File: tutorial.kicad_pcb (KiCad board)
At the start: 2 copper layers, 174.4 x 164.8 mm, 64 parts

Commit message: modified the pcb some
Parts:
- moved TRRS1 9.19 mm to (214.5, 130.5)
- moved _1 3.21 mm to (210.7, 92.6)
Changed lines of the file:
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@@
 		(fp_line
 			(start -0.35 0)
-			(end -0.35 0.550001)
+			(end -0.35 0.550002)
 			(stroke
 				(width 0.1)
@@
 		(fp_line
 			(start -0.35 0)
-			(end -0.35 0.550001)
+			(end -0.35 0.550002)
 			(stroke
 				(width 0.1)
@@
 		(fp_line
 			(start -0.35 0)
-			(end -0.35 0.550001)
+			(end -0.35 0.550002)
 			(stroke
 				(width 0.1)
@@
 		(fp_line
 			(start -0.35 0)
-			(end -0.35 0.550001)
+			(end -0.35 0.550002)
 			(stroke
 				(width 0.1)
@@
 		(fp_line
 			(start -0.35 0)
-			(end -0.35 0.550001)
+			(end -0.35 0.550002)
 			(stroke
 				(width 0.1)
@@
 		(fp_line
 			(start -0.35 0)
-			(end -0.35 0.550001)
+			(end -0.35 0.550002)
 			(stroke
 				(width 0.1)
@@
 		(fp_line
 			(start -0.35 0)
-			(end -0.35 0.550001)
+			(end -0.35 0.550002)
 			(stroke
 				(width 0.1)
@@
 		(fp_line
 			(start -0.35 0)
-			(end -0.35 0.550001)
+			(end -0.35 0.550002)
 			(stroke
 				(width 0.1)
@@
 		(fp_line
 			(start -0.35 0)
-			(end -0.35 0.550001)
+			(end -0.35 0.550002)
 			(stroke
 				(width 0.1)
@@
 		(fp_line
 			(start -0.35 0)
-			(end -0.35 0.550001)
+			(end -0.35 0.550002)
 			(stroke
 				(width 0.1)
@@
 		(fp_line
 			(start -0.35 0)
-			(end -0.35 0.550001)
+			(end -0.35 0.550002)
 			(stroke
 				(width 0.1)
@@
 		(fp_line
 			(start -0.35 0)
-			(end -0.35 0.550001)
+			(end -0.35 0.550002)
 			(stroke
 				(width 0.1)
@@
 		(fp_line
 			(start -0.35 0)
-			(end -0.35 0.550001)
+			(end -0.35 0.550002)
 			(stroke
 				(width 0.1)
@@
 		(fp_line
 			(start -0.35 0)
-			(end -0.35 0.550001)
+			(end -0.35 0.550002)
 			(stroke
 				(width 0.1)
@@
 		(fp_line
 			(start -0.35 0)
-			(end -0.35 0.550001)
+			(end -0.35 0.550002)
 			(stroke
 				(width 0.1)
@@
 		(fp_line
 			(start -0.35 0)
-			(end -0.35 0.550001)
+			(end -0.35 0.550002)
 			(stroke
 				(width 0.1)
@@
 	(footprint "RPi_Pico_SMD_TH"
 		(layer "F.Cu")
-		(at 209.404157 95.553697 -15)
+		(at 210.730194 92.627828 -15)
 		(property "Reference" "_1"
 			(at 0 0 0)
@@
 			)
 		)
-		(fp_text user "Copper Keepouts shown on Dwgs layer"
-			(at 0.1 -30.2 0)
-			(layer "Cmts.User")
-			(effects
-				(font
-					(size 1 1)
-					(thickness 0.15)
-				)
-			)
-		)
 		(fp_text user "${REFERENCE}"
 			(at 0 0 180)
@@
 		(fp_line
 			(start -0.35 0)
-			(end -0.35 0.550001)
+			(end -0.35 0.550002)
 			(stroke
 				(width 0.1)
@@
 		(fp_line
 			(start -0.35 0)
-			(end -0.35 0.550001)
+			(end -0.35 0.550002)
 			(stroke
 				(width 0.1)
@@
 		(fp_line
 			(start -0.35 0)
-			(end -0.35 0.550001)
+			(end -0.35 0.550002)
 			(stroke
 				(width 0.1)
@@
 		(fp_line
 			(start -0.35 0)
-			(end -0.35 0.550001)
+			(end -0.35 0.550002)
 			(stroke
 				(width 0.1)
@@
 		(fp_line
 			(start -0.35 0)
-			(end -0.35 0.550001)
+			(end -0.35 0.550002)
 			(stroke
 				(width 0.1)
@@
 		(fp_line
 			(start -0.35 0)
-			(end -0.35 0.550001)
+			(end -0.35 0.550002)
 			(stroke
 				(width 0.1)
@@
 		(fp_line
 			(start -0.35 0)
-			(end -0.35 0.550001)
+			(end -0.35 0.550002)
 			(stroke
 				(width 0.1)
@@
 		(fp_line
 			(start -0.35 0)
-			(end -0.35 0.550001)
+			(end -0.35 0.550002)
 			(stroke
 				(width 0.1)
@@
 		(fp_line
 			(start -0.35 0)
-			(end -0.35 0.550001)
+			(end -0.35 0.550002)
 			(stroke
 				(width 0.1)
@@
 		(fp_line
 			(start -0.35 0)
-			(end -0.35 0.550001)
+			(end -0.35 0.550002)
 			(stroke
 				(width 0.1)
@@
 		(fp_line
 			(start -0.35 0)
-			(end -0.35 0.550001)
+			(end -0.35 0.550002)
 			(stroke
 				(width 0.1)
@@
 		(fp_line
 			(start -0.35 0)
-			(end -0.35 0.550001)
+			(end -0.35 0.550002)
 			(stroke
 				(width 0.1)
@@
 	(footprint "ceoloide:trrs_pj320a (reversible, symmetric)"
 		(layer "F.Cu")
-		(at 209.306933 122.962465 -105)
+		(at 214.495679 130.54985 -105)
 		(property "Reference" "TRRS1"
 			(at 0 14.2 -105)
@@
 		)
 		(pad "2" thru_hole oval
-			(at 2.299999 3.2 255)
+			(at 2.299998 3.2 255)
 			(size 1.6 2.2)
 			(drill oval 0.9 1.5)
@@
 		(fp_line
 			(start -0.35 0)
-			(end -0.35 0.550001)
+			(end -0.35 0.550002)
 			(stroke
 				(width 0.1)
@@
 		(fp_line
 			(start -0.35 0)
-			(end -0.35 0.550001)
+			(end -0.35 0.550002)
 			(stroke
 				(width 0.1)
@@
 		(fp_line
 			(start -0.35 0)
-			(end -0.35 0.550001)
+			(end -0.35 0.550002)
 			(stroke
 				(width 0.1)
@@
 		(fp_line
 			(start -0.35 0)
-			(end -0.35 0.550001)
+			(end -0.35 0.550002)
 			(stroke
 				(width 0.1)
@@
 		(fp_line
 			(start -0.35 0)
-			(end -0.35 0.550001)
+			(end -0.35 0.550002)
 			(stroke
 				(width 0.1)
@@
 		(fp_line
 			(start -0.35 0)
-			(end -0.35 0.550001)
+			(end -0.35 0.550002)
 			(stroke
 				(width 0.1)
@@
 		(fp_line
 			(start -0.35 0)
-			(end -0.35 0.550001)
+			(end -0.35 0.550002)
 			(stroke
 				(width 0.1)
@@
 		(fp_line
 			(start -0.35 0)
-			(end -0.35 0.550001)
+			(end -0.35 0.550002)
 			(stroke
 				(width 0.1)
@@
 		(fp_line
 			(start -0.35 0)
-			(end -0.35 0.550001)
+			(end -0.35 0.550002)
 			(stroke
 				(width 0.1)
@@
 		(fp_line
 			(start -0.35 0)
-			(end -0.35 0.550001)
+			(end -0.35 0.550002)
 			(stroke
 				(width 0.1)
@@
 		(fp_line
 			(start -0.35 0)
-			(end -0.35 0.550001)
+			(end -0.35 0.550002)
 			(stroke
 				(width 0.1)
@@
 		(fp_line
 			(start -0.35 0)
-			(end -0.35 0.550001)
+			(end -0.35 0.550002)
 			(stroke
 				(width 0.1)
@@
 		(fp_line
 			(start -0.35 0)
-			(end -0.35 0.550001)
+			(end -0.35 0.550002)
 			(stroke
 				(width 0.1)
@@
 		(fp_line
 			(start -0.35 0)
-			(end -0.35 0.550001)
+			(end -0.35 0.550002)
 			(stroke
 				(width 0.1)
@@
 		(fp_line
 			(start -0.35 0)
-			(end -0.35 0.550001)
+			(end -0.35 0.550002)
 			(stroke
 				(width 0.1)
@@
 		(fp_line
 			(start -0.35 0)
-			(end -0.35 0.550001)
+			(end -0.35 0.550002)
 			(stroke
 				(width 0.1)
@@
 		(fp_line
 			(start -0.35 0)
-			(end -0.35 0.550001)
+			(end -0.35 0.550002)
 			(stroke
 				(width 0.1)
@@
 		(fp_line
 			(start -0.35 0)
-			(end -0.35 0.550001)
+			(end -0.35 0.550002)
 			(stroke
 				(width 0.1)
@@
 		(fp_line
 			(start -0.35 0)
-			(end -0.35 0.550001)
+			(end -0.35 0.550002)
 			(stroke
 				(width 0.1)
@@
 		(fp_line
 			(start -0.35 0)
-			(end -0.35 0.550001)
+			(end -0.35 0.550002)
 			(stroke
 				(width 0.1)
@@
 		(fp_line
 			(start -0.35 0)
-			(end -0.35 0.550001)
+			(end -0.35 0.550002)
 			(stroke
 				(width 0.1)
@@
 		(fp_line
 			(start -0.35 0)
-			(end -0.35 0.550001)
+			(end -0.35 0.550002)
 			(stroke
 				(width 0.1)
@@
 		(fp_line
 			(start -0.35 0)
-			(end -0.35 0.550001)
+			(end -0.35 0.550002)
 			(stroke
 				(width 0.1)
@@
 		(fp_line
 			(start -0.35 0)
-			(end -0.35 0.550001)
+			(end -0.35 0.550002)
 			(stroke
 				(width 0.1)
@@
 		(fp_line
 			(start -0.35 0)
-			(end -0.35 0.550001)
+			(end -0.35 0.550002)
 			(stroke
 				(width 0.1)
@@
 		(fp_line
 			(start -0.35 0)
-			(end -0.35 0.550001)
+			(end -0.35 0.550002)
 			(stroke
 				(width 0.1)
@@
 		(fp_line
 			(start -0.35 0)
-			(end -0.35 0.550001)
+			(end -0.35 0.550002)
 			(stroke
 				(width 0.1)
@@
 		(fp_line
 			(start -0.35 0)
-			(end -0.35 0.550001)
+			(end -0.35 0.550002)
 			(stroke
 				(width 0.1)

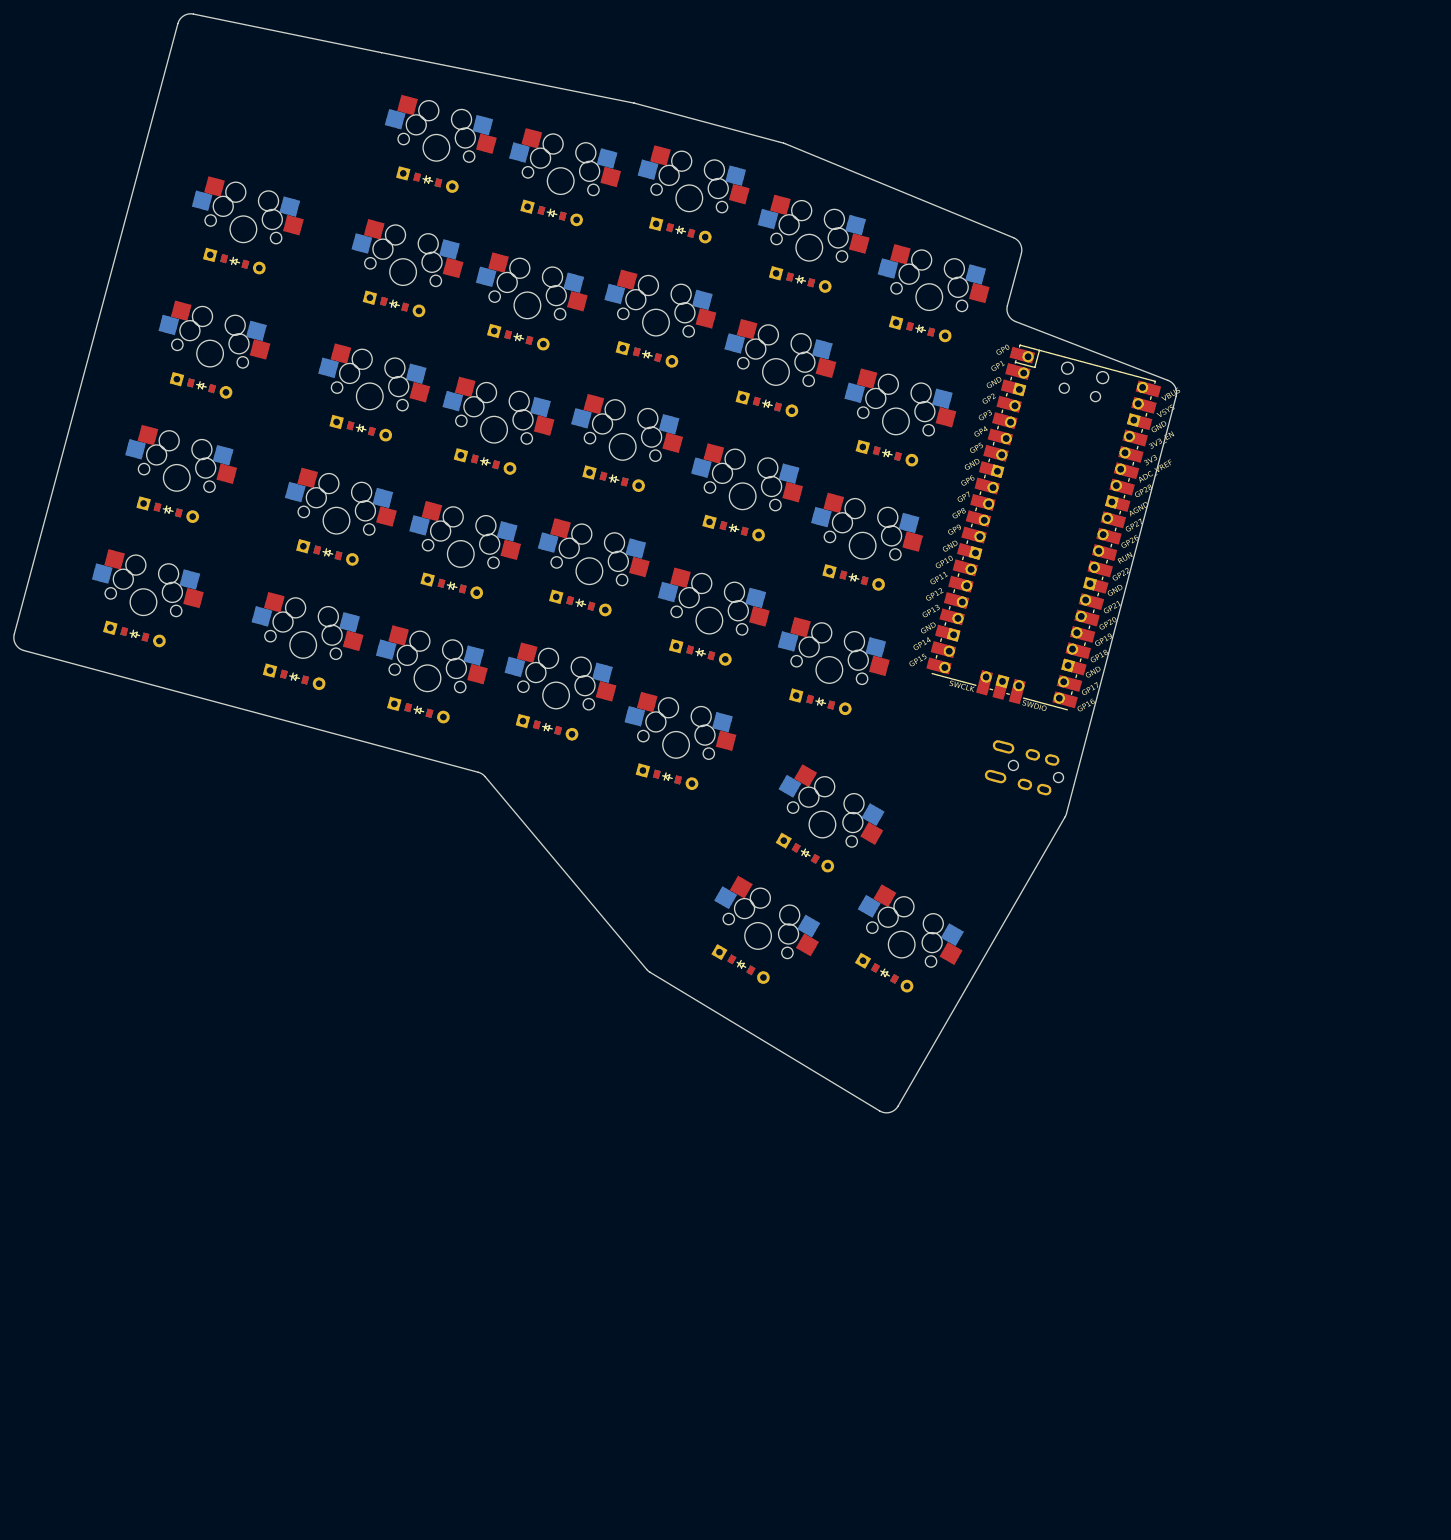
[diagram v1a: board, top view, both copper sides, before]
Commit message: fixed positioning for pico and trrs, added oled
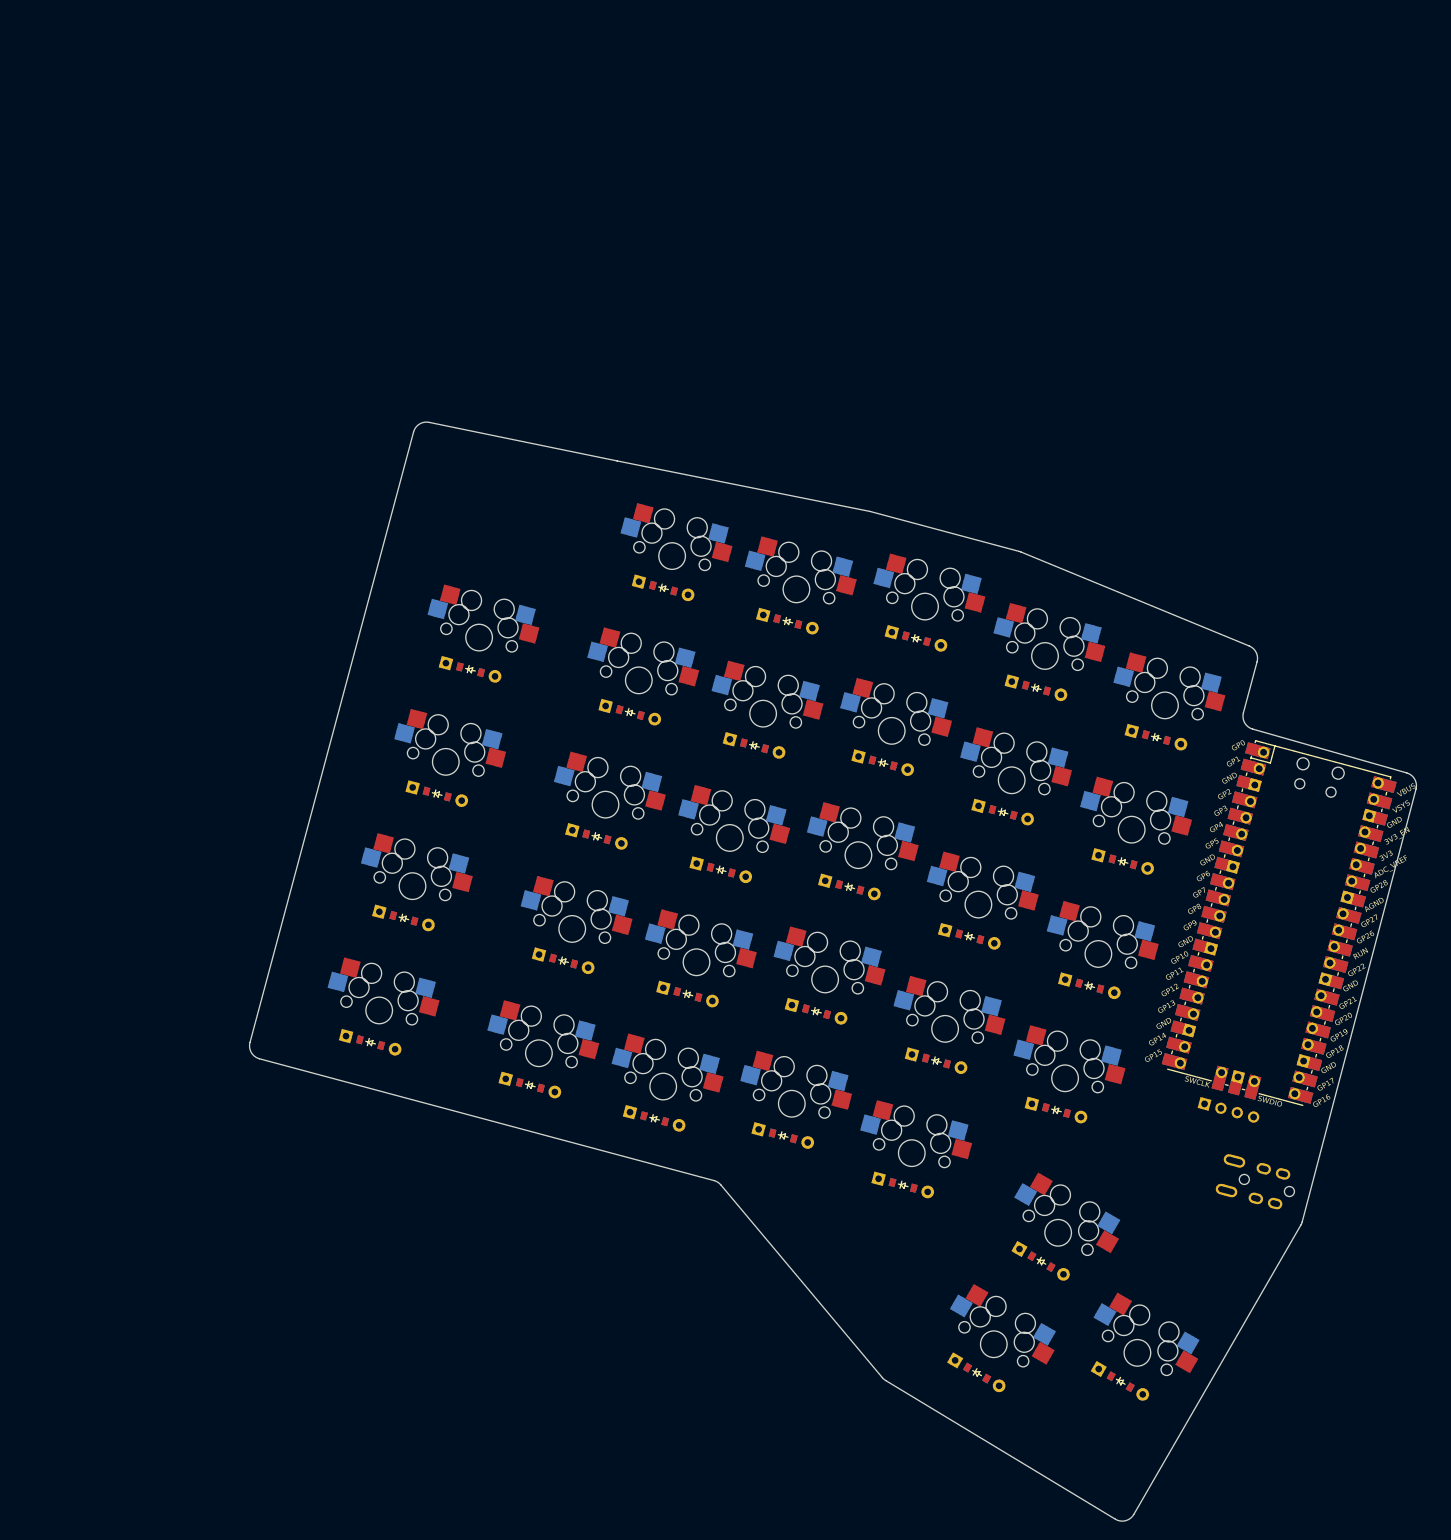
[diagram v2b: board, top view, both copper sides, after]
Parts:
- removed the _1 at (210.7, 92.6)
- added OLED1: OLED, lib:OLED_headers, F.Cu at (244.7, 180.1)
- added _1 (x2): RPi_Pico_SMD_TH, RPi_Pico_SMD_TH, F.Cu at (246.1, 152.0)
- moved TRRS1 71.1 mm to (249.1, 192.6)
- moved S18 70.7 mm to (187.9, 123.1)
- moved D28 70.7 mm to (227.6, 124.1)
- moved S4 70.7 mm to (126.0, 109.1)
- moved D18 70.7 mm to (186.6, 128.0)
- moved D29 70.7 mm to (200.7, 219.5)
- moved D31 70.7 mm to (222.3, 220.8)
- moved S21 70.7 mm to (195.9, 167.8)
- moved S29 70.7 mm to (203.2, 215.1)
- moved S31 70.7 mm to (224.8, 216.4)
- moved D11 70.7 mm to (157.4, 162.7)
- moved D13 70.7 mm to (167.4, 125.4)
- moved D14 70.7 mm to (172.3, 106.7)
- moved D4 70.7 mm to (124.8, 114.0)
- moved D7 70.7 mm to (143.7, 139.0)
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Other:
- board size 174.4 x 164.8 mm -> 175 x 164.8 mm

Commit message: add reset buttons
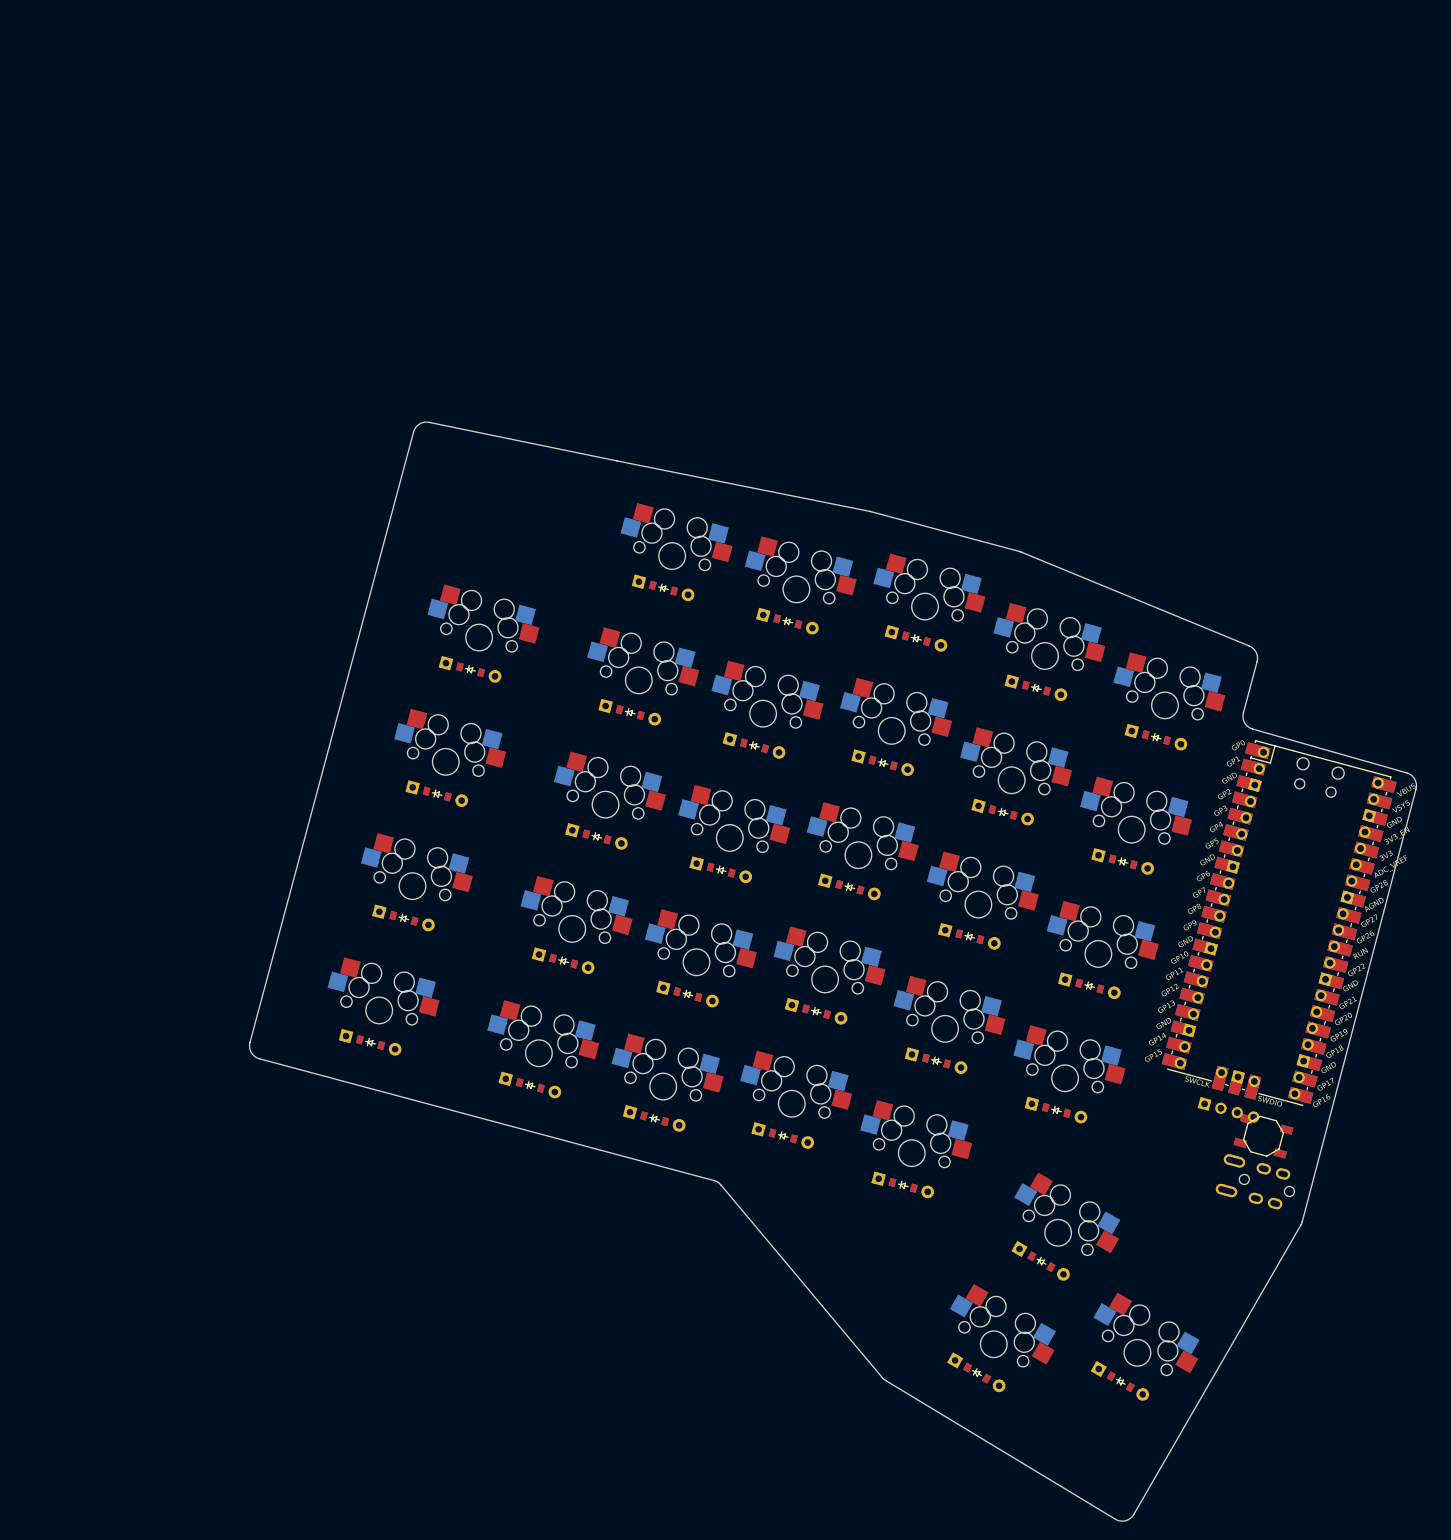
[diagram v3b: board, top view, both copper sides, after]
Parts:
- removed the _1 at (246.1, 152.0) (x2)
- added B1, B2: , E73:SW_TACT_ALPS_SKQGABE010, F.Cu at (243.7, 183.9)
- added _1 (x2): RPi_Pico_SMD_TH, RPi_Pico_SMD_TH, F.Cu at (246.1, 152.0)
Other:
- net class Default added: clearance 0.2, trace_width 0.25, via_dia 0.8, via_drill 0.4
